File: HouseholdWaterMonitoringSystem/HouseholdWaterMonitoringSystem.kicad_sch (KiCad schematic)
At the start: 8 parts

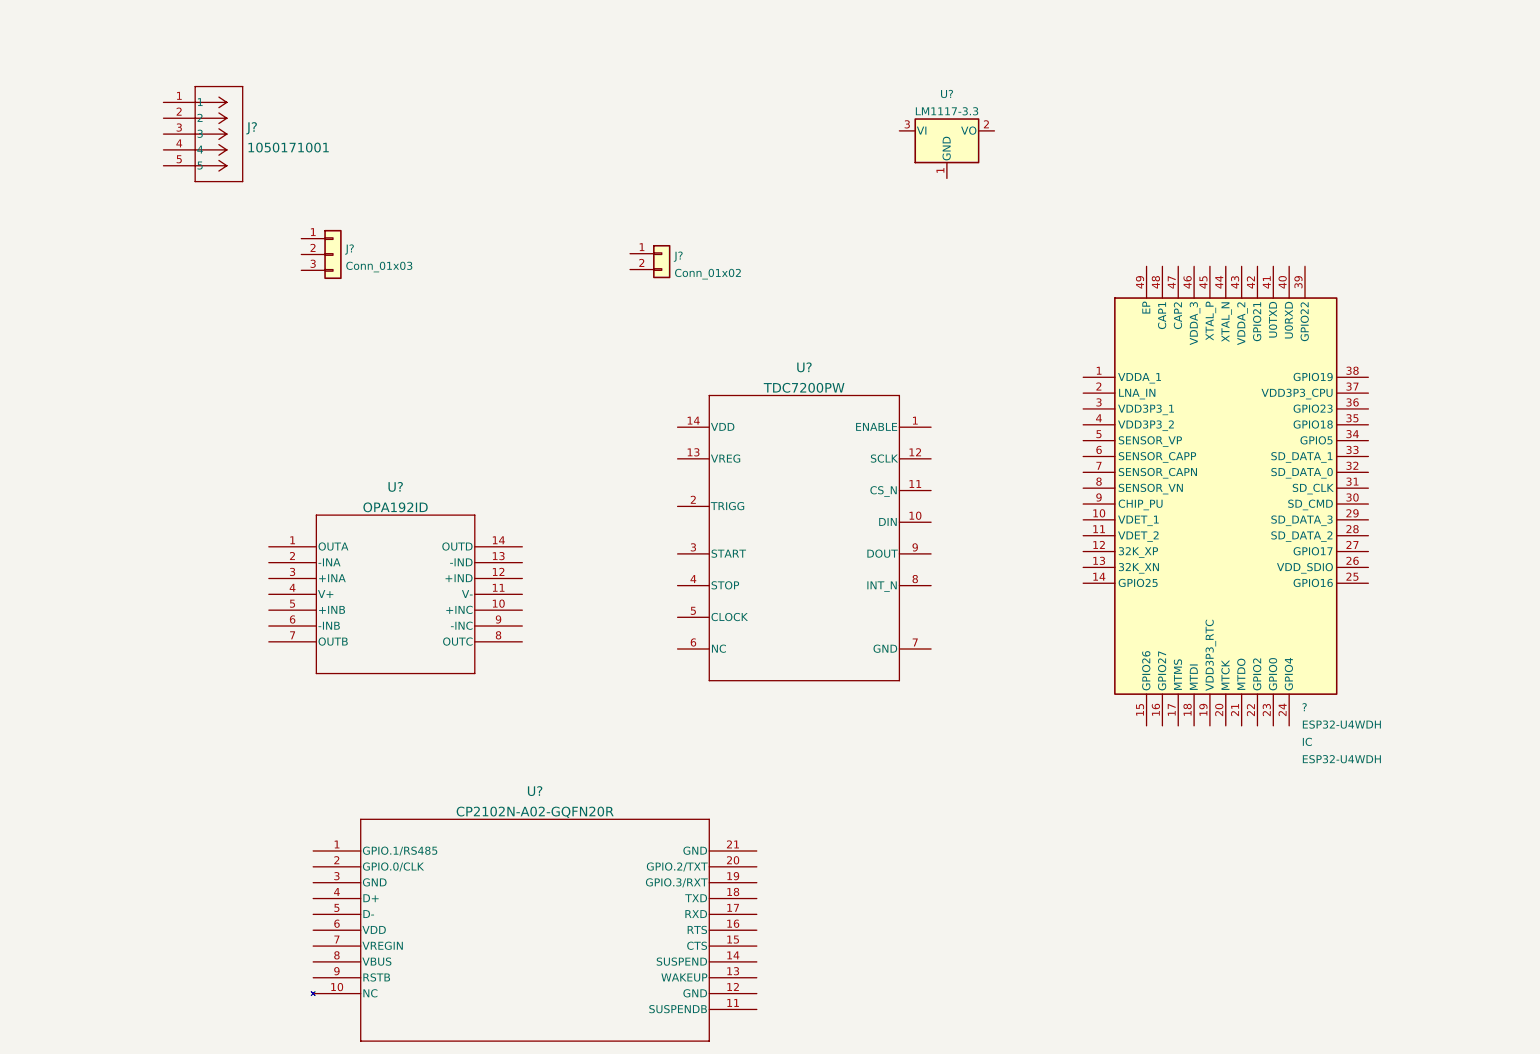
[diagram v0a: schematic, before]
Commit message: modified parts' pinouts
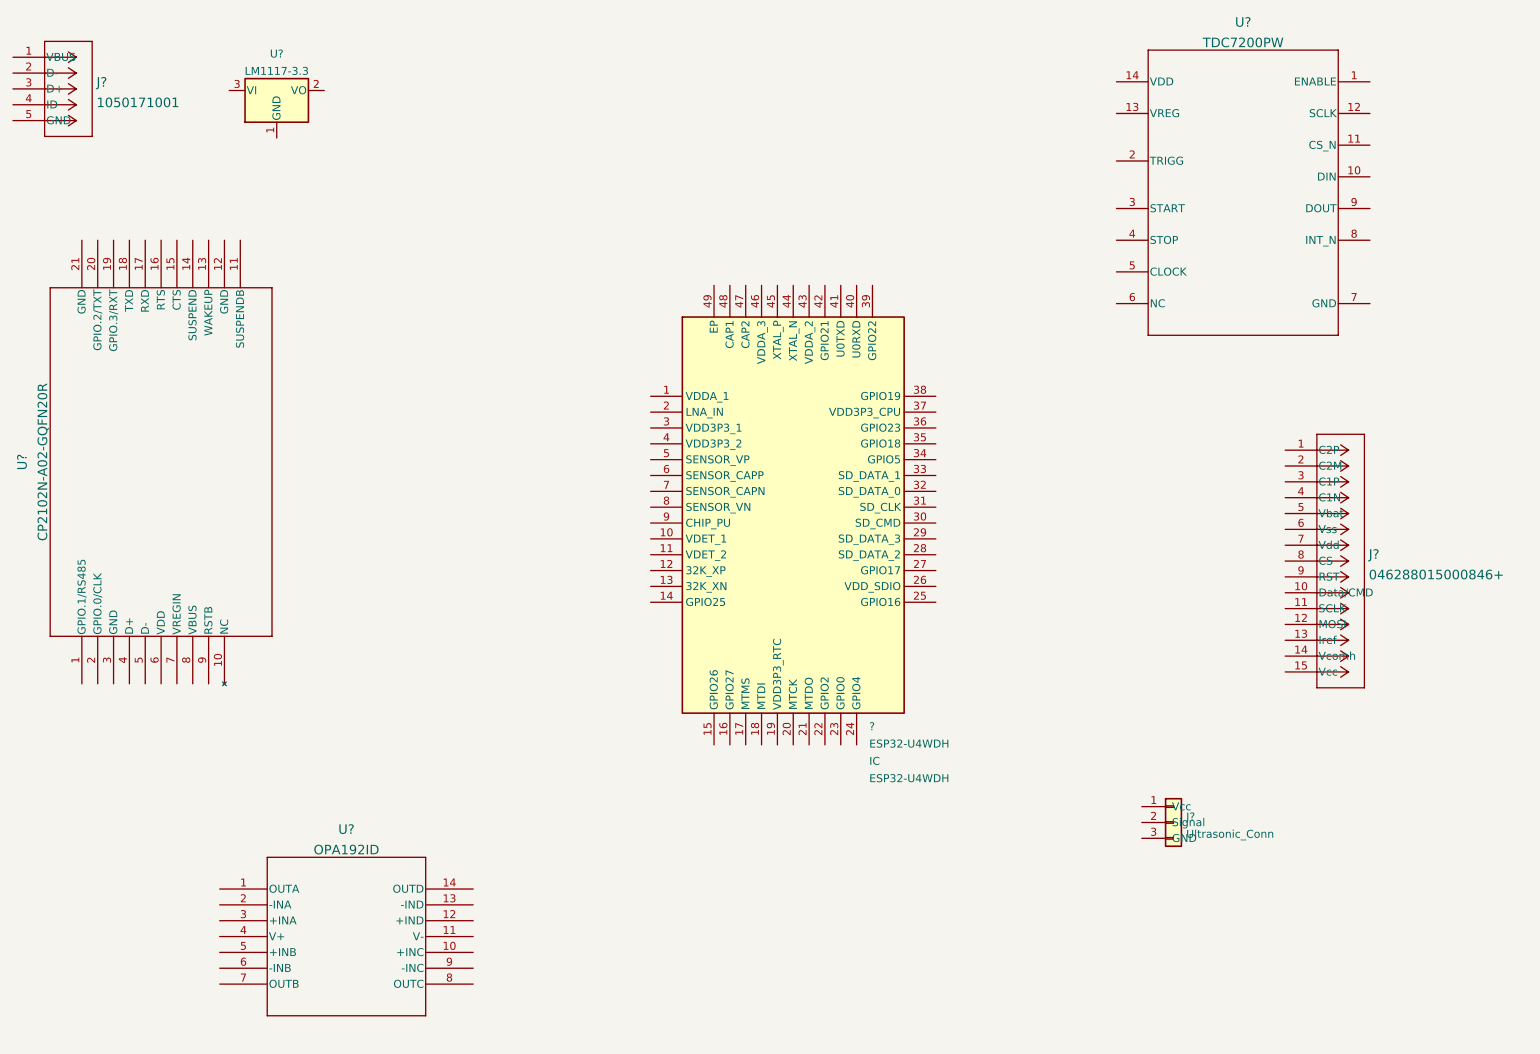
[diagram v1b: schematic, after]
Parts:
- removed J?: Conn_01x02, symbol Connector_Generic:Conn_01x02
- added J?: 046288015000846+, CONN15_6288_7X5P7_AVX, symbol 15-pin_ZIF_connector:046288015000846+
- J?: value Conn_01x03 -> Ultrasonic_Conn
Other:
- moved on the sheet: ?, J?, U?
